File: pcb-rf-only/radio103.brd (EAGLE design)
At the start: 99 x 100 mm, 71 parts, among them IC1 LM833D, IC2 7805TV, IC3 74ACT00D, IC5 LM386M-1, IC6 LM1117MPX-3.3, J1 PJ-324MH, J2 PJ-324MH, J3 PJ-324MH, U1 FST3253

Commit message: MCP encoder + mic amp
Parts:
- added C28, C31: 100n, rcl:C0805K
- added C29, C30, C32: (no value), rcl:E2,5-6E
- added IC7: 4066D, 40xx:SO14
- added IC8: LM833D, linear:SO08
- added JP4: (no value), pinhead:1X02
- added R34, R35, R36, R37, R38, R39, R40: (no value), rcl:R0805
- moved U$2 13.6 mm to (70.4, 55.5)
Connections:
- new net MIC: IC7.8
- new net N$48: C30.+, IC8.3, R35.2, R36.1
- new net N$49: C31.1, IC8.2, R34.2, R37.2
- new net N$50: C31.2, IC8.1, R34.1, R39.2
- new net N$51: C29.-, R37.1
- new net N$52: C29.+, JP4.2, R38.2
- new net N$53: C32.-, R39.1
- new net N$54: C32.+, R40.1
- new net RXEN: IC7.13, IC7.5
- new net RX_I: IC7.1
- new net RX_Q: IC7.4
- new net TXEN: IC7.12, IC7.6
- new net VDD: IC7.14
- new net VSS: IC7.7
- net ADC_RX_I: now also IC7.2, IC7.9
- net ADC_RX_Q: now also IC7.10, IC7.3
- net GND: now also C28.1, C30.-, IC7.11, IC8.4, JP4.1, R36.2, R40.2
- net VOPAMP: now also C28.2, IC8.8, R35.1, R38.1

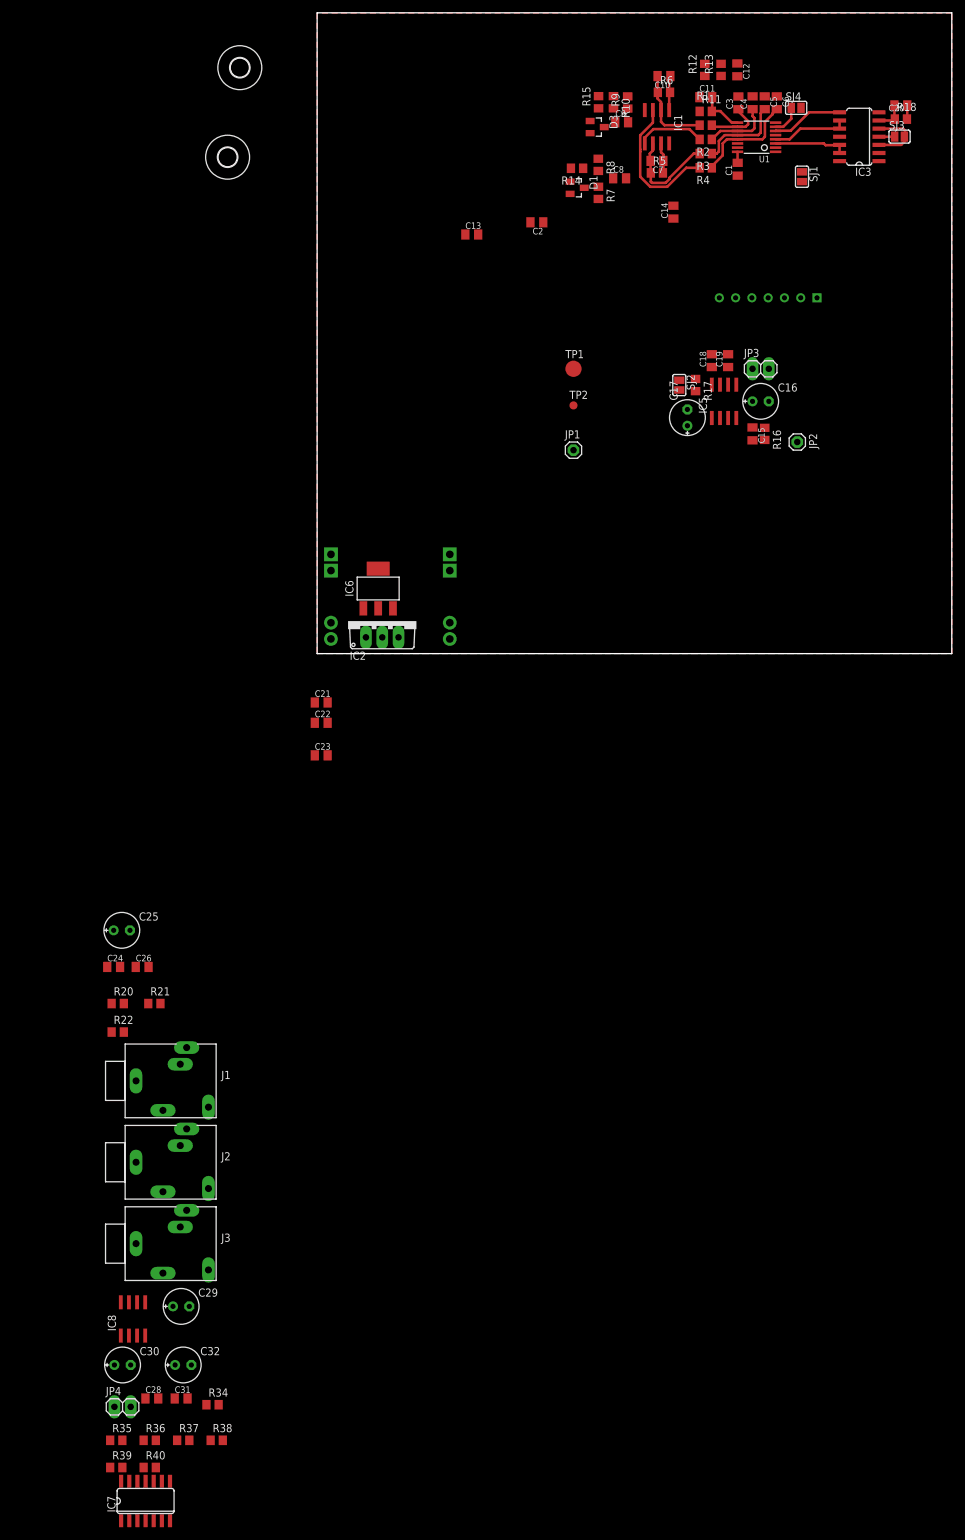
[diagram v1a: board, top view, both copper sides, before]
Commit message: fonts + font generator + UI layout
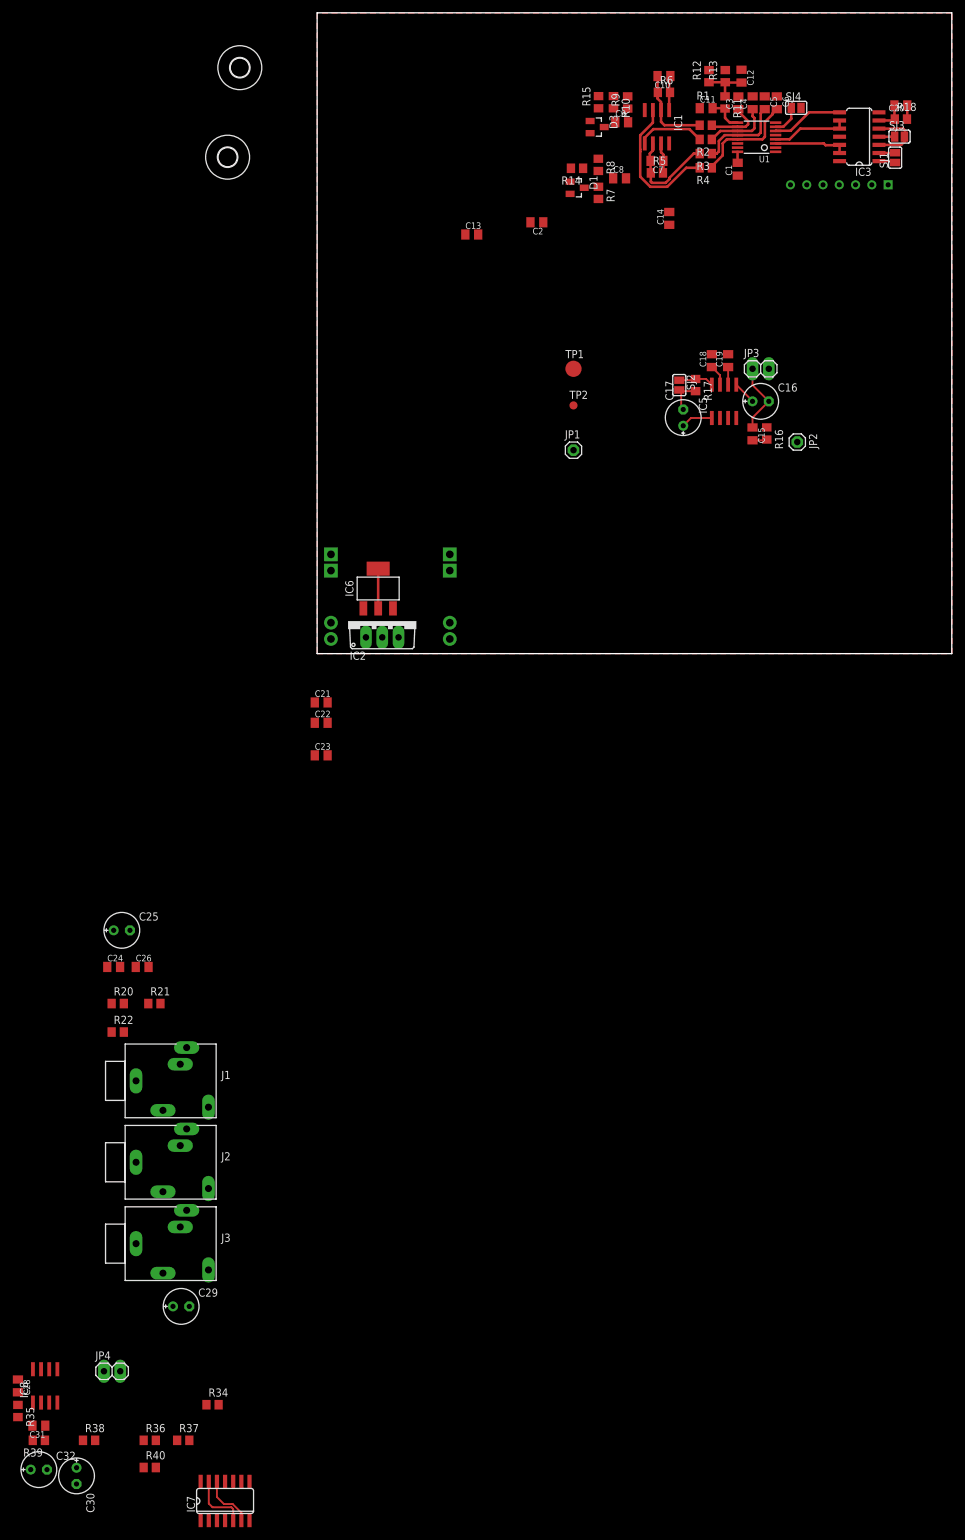
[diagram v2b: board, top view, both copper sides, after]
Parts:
- moved C32 27.8 mm to (-43.4, -127.3)
- moved C31 22.6 mm to (-43.4, -120.5), turned to 180 degrees
- moved C28 21.0 mm to (-46.7, -114.3), turned to 270 degrees
- moved U$2 20.8 mm to (81.5, 73.2)
- moved R38 19.9 mm to (-35.6, -122.8)
- moved C30 18.7 mm to (-37.5, -128.3), turned to 270 degrees
- moved IC8 17.2 mm to (-42.4, -114.3)
- moved R35 16.0 mm to (-46.7, -118.2), turned to 270 degrees
- moved SJ1 14.8 mm to (90.2, 77.4), turned to 90 degrees
- moved R39 12.8 mm to (-43.4, -122.8), turned to 180 degrees
- moved IC7 12.4 mm to (-14.4, -132.2)
- moved JP4 5.79 mm to (-32.0, -112.0)
- moved R11 3.32 mm to (63.7, 86.0), turned to 270 degrees
- moved C11 1.72 mm to (60.7, 85.1)
- moved C14 1.18 mm to (54.9, 67.9)
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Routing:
- net N$24: track 0.00 -> 11.3 mm
- net RXEN: track 0.00 -> 9.45 mm
- net TXEN: track 0.00 -> 8.54 mm
- net N$14: track 0.00 -> 7.32 mm
- net 3V3: track 1.73 -> 7.93 mm
- net N$21: track 0.00 -> 5.61 mm
- net N$20: track 0.00 -> 5.53 mm
- net N$19: track 0.00 -> 4.96 mm
- net N$23: track 0.00 -> 3.65 mm
- net N$22: track 0.00 -> 3.28 mm
- net 5V: track 0.00 -> 2.75 mm
- net N$27: track 0.00 -> 2.61 mm
- net N$26: track 0.00 -> 2.54 mm
- net N$25: track 0.00 -> 2.27 mm
